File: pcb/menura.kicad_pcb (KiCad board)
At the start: 2 copper layers, 123.3 x 97.2 mm, 54 parts, among them SW1 SW_Push, SW10 SW_Push, SW11 SW_Push, SW12 SW_Push, SW13 SW_Push, SW14 SW_Push, SW15 SW_Push, SW16 SW_Push, SW17 SW_Push, SW18 SW_Push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

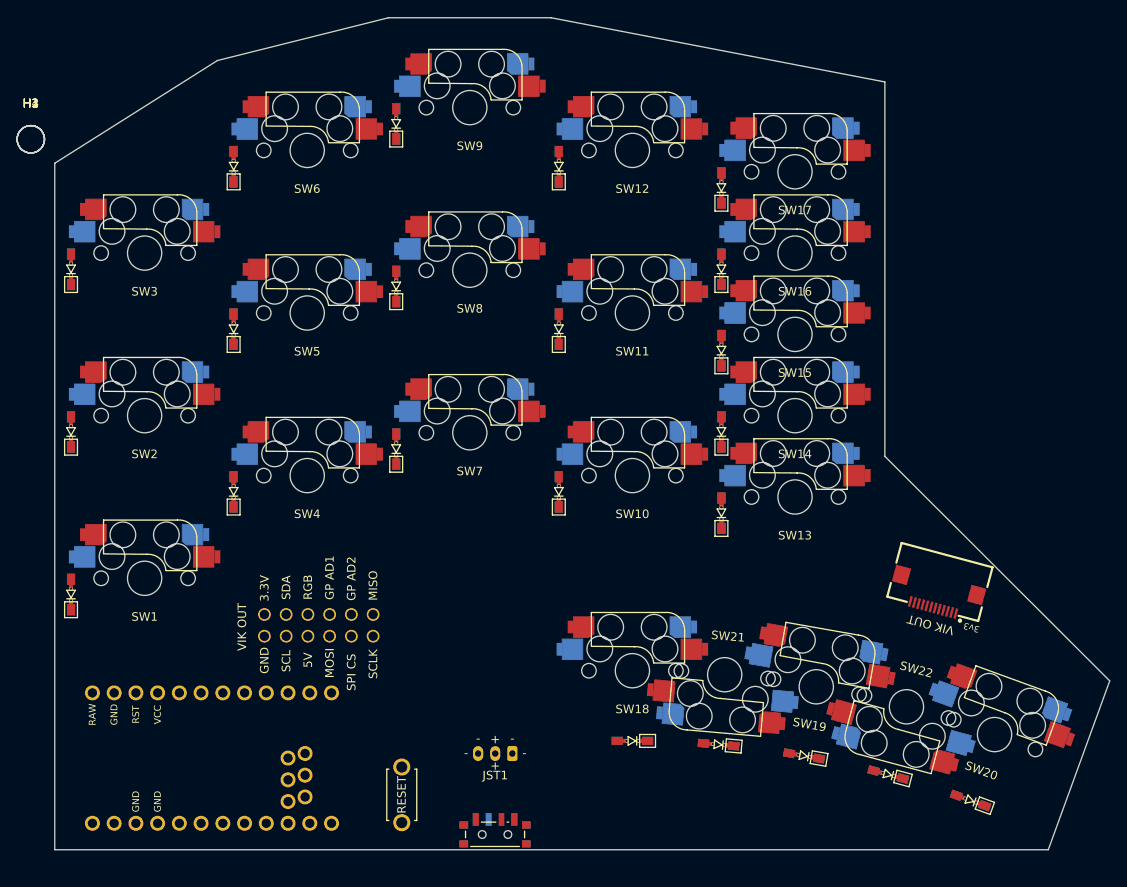
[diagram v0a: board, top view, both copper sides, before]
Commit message: adjust vik position and rotation
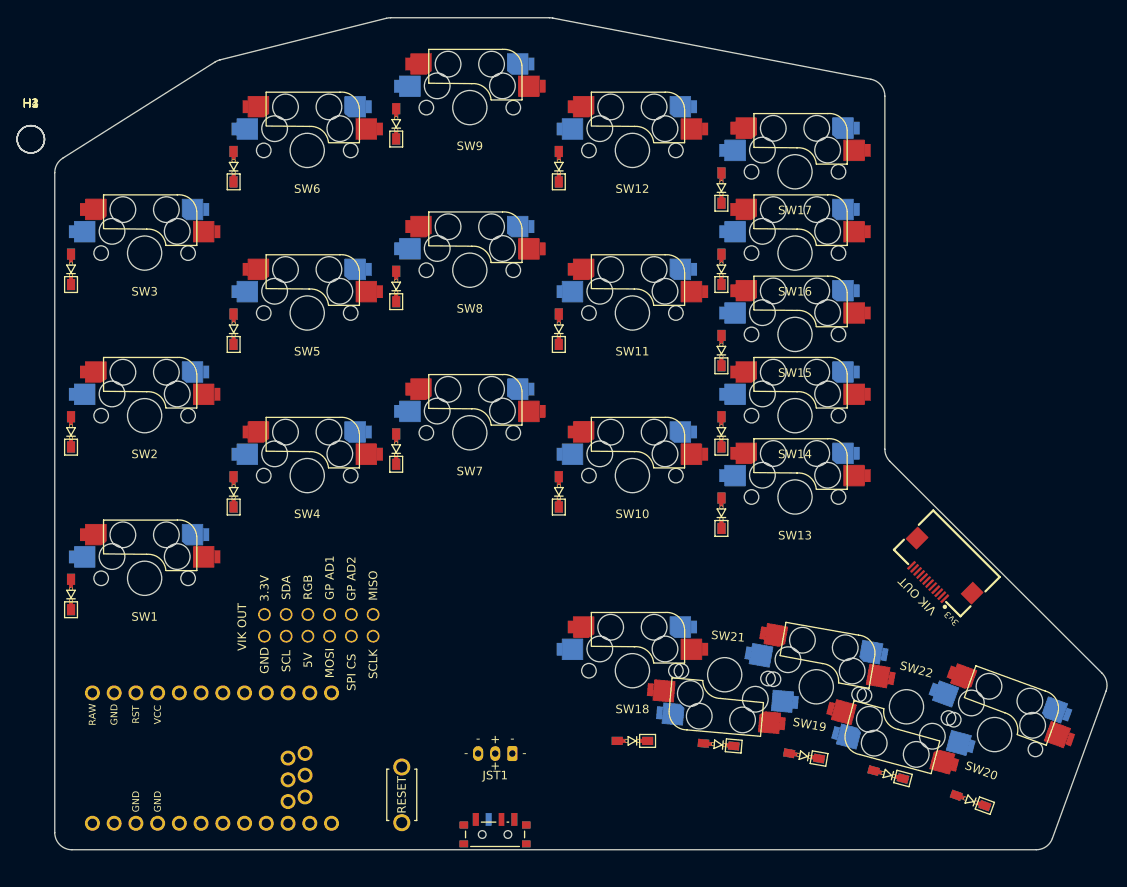
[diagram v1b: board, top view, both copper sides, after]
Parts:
- moved VIK1 2.47 mm to (193.0, 99.0), turned to 135 degrees
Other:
- board size 123.3 x 97.2 mm -> 123 x 97.2 mm

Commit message: shuffle few components around
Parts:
- moved JST1 28.0 mm to (116.5, 104.3), turned to 90 degrees
- moved VIK2 19.3 mm to (135.5, 115.5), turned to -90 degrees
- moved RSW1 13.0 mm to (142.3, 129.7), turned to 0 degrees
- moved PWR1 9.52 mm to (131.4, 129.9)

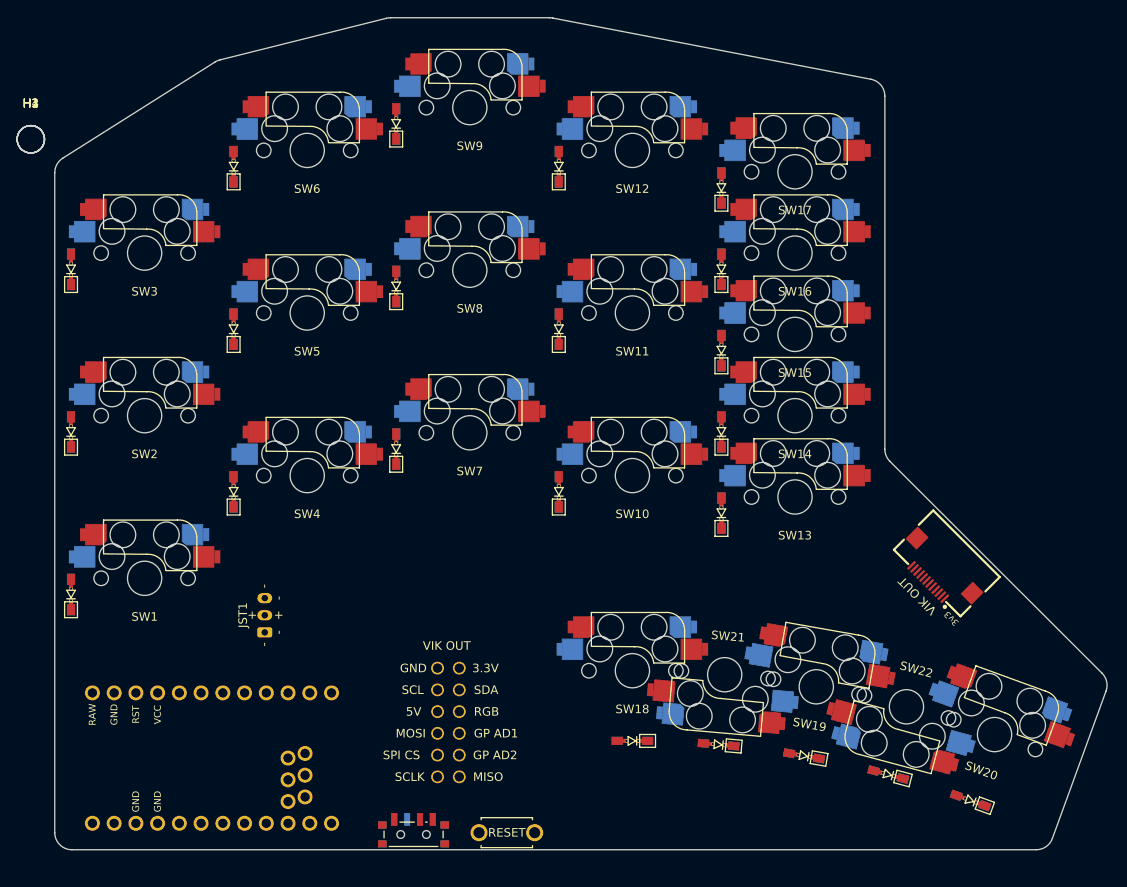
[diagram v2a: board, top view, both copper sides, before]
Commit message: tweak urchin diode footprint, add tenting puck footprints
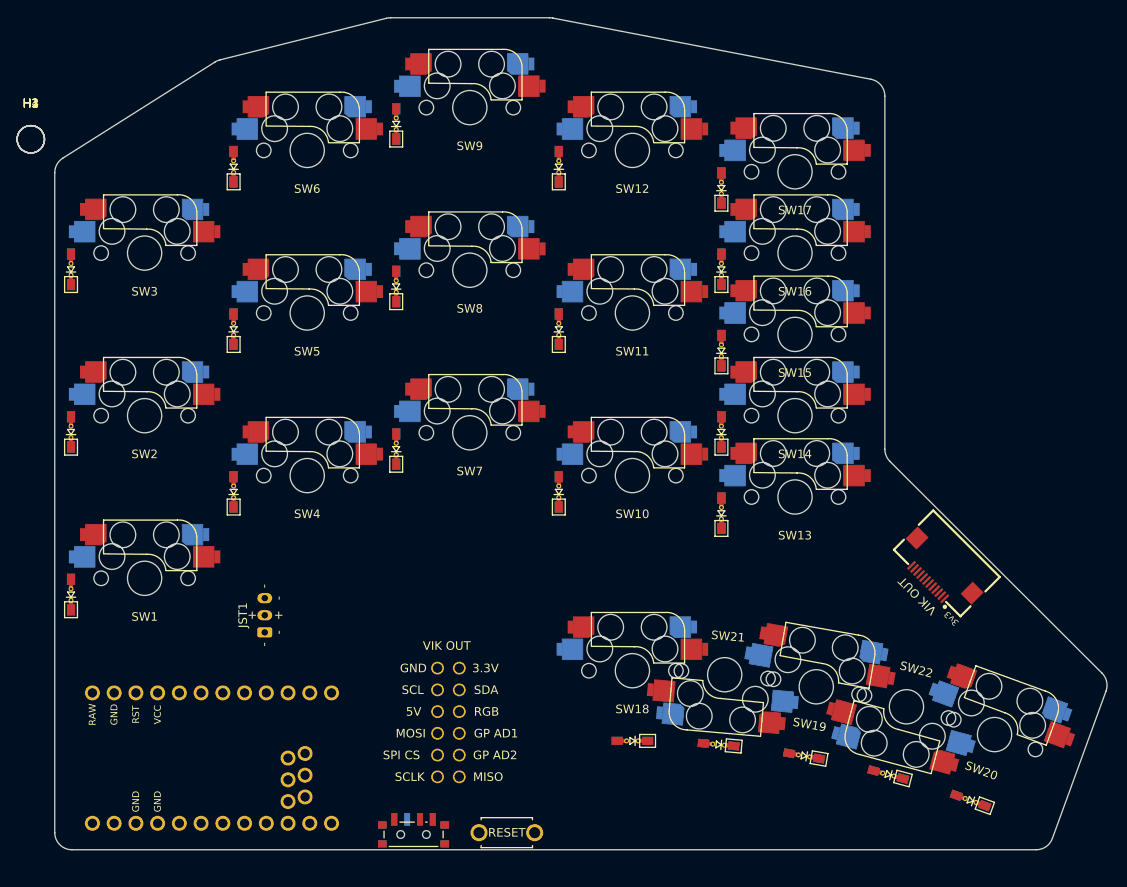
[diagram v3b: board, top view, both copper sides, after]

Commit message: logo silkscreens
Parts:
- added LOGO1: menura, quappo:Logo_menura, F.Cu at (167.3, 129.7)
- added LOGO2: vik, quappo:Logo_vik-small, F.Cu at (200.7, 105.4)

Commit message: holes
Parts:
- D1, D10, D11, D12, D13, D14, D15, D16, D17, D18, D19, D2, D20, D21, D22, D3, D4, D5, D6, D7, D8, D9: value 1N4148W -> (none); footprint quappo:Diode_SMD-reversible-urchin -> ComboDiode
- H1, H2, H3, H4: value MountingHole -> (none); footprint MountingHole:MountingHole_3.2mm_M3 -> SMDPad
- JST1: value Conn_01x03_Socket -> (none); footprint quappo:Connector_JST-PH-3prong -> JST_PH_S2B-PH-K_02x2.00mm_Angled
- LOGO1: value menura -> (none); footprint quappo:Logo_menura -> SMDPad
- LOGO2: value vik -> (none); footprint quappo:Logo_vik-small -> SMDPad
- MCU1: value N!N -> (none); footprint quappo:MCU_nice-nano -> ProMicro
- PWR1: value SW_SPDT -> (none); footprint quappo:Switch_power-reversible-kim -> E73:SPDT_C128955
- RSW1: value SW_Push -> (none); footprint quappo:Switch_reset-2pin -> E73:SW_TACT_ALPS_SKQGABE010
- SW1, SW10, SW11, SW12, SW13, SW14, SW15, SW16, SW17, SW18, SW19, SW2, SW20, SW21, SW22, SW3, SW4, SW5, SW6, SW7, SW8, SW9: value SW_Push -> (none); footprint quappo:Switch_MX-hotswap-reversible -> MX
- VIK1: value ~ -> (none); footprint quappo:Connector_vik-keyboard-horizontal -> SMDPad
- VIK2: value ~ -> (none); footprint quappo:Connector_vik-keyboard-throughhole -> SMDPad
- moved LOGO2 47.5 mm to (157.3, 124.7), turned to 360 degrees
- moved VIK1 5.66 mm to (197.0, 103.0)
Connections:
- D1 pad 1: row2 -> (no net)
- D1 pad 2: Net-(D1-A) -> (no net)
- D10 pad 1: row2 -> (no net)
- D10 pad 2: Net-(D10-A) -> (no net)
- D11 pad 1: row1 -> (no net)
- D11 pad 2: Net-(D11-A) -> (no net)
- D12 pad 1: row0 -> (no net)
- D12 pad 2: Net-(D12-A) -> (no net)
- D13 pad 1: row2 -> (no net)
- D13 pad 2: Net-(D13-A) -> (no net)
- D14 pad 1: row1 -> (no net)
- D14 pad 2: Net-(D14-A) -> (no net)
- D15 pad 1: row1 -> (no net)
- D15 pad 2: Net-(D15-A) -> (no net)
- D16 pad 1: row0 -> (no net)
- D16 pad 2: Net-(D16-A) -> (no net)
- D17 pad 1: row0 -> (no net)
- D17 pad 2: Net-(D17-A) -> (no net)
- D18 pad 1: row3 -> (no net)
- D18 pad 2: Net-(D18-A) -> (no net)
- D19 pad 1: row3 -> (no net)
- D19 pad 2: Net-(D19-A) -> (no net)
- D2 pad 1: row1 -> (no net)
- D2 pad 2: Net-(D2-A) -> (no net)
- D20 pad 1: row3 -> (no net)
- D20 pad 2: Net-(D20-A) -> (no net)
- D21 pad 1: row3 -> (no net)
- D21 pad 2: Net-(D21-A) -> (no net)
- D22 pad 1: row3 -> (no net)
- D22 pad 2: Net-(D22-A) -> (no net)
- D3 pad 1: row0 -> (no net)
- D3 pad 2: Net-(D3-A) -> (no net)
- D4 pad 1: row2 -> (no net)
- D4 pad 2: Net-(D4-A) -> (no net)
- D5 pad 1: row1 -> (no net)
- D5 pad 2: Net-(D5-A) -> (no net)
- D6 pad 1: row0 -> (no net)
- D6 pad 2: Net-(D6-A) -> (no net)
- D7 pad 1: row2 -> (no net)
- D7 pad 2: Net-(D7-A) -> (no net)
- D8 pad 1: row1 -> (no net)
- D8 pad 2: Net-(D8-A) -> (no net)
- D9 pad 1: row0 -> (no net)
- D9 pad 2: Net-(D9-A) -> (no net)
- JST1 pad 1: GND -> (no net)
- JST1 pad 2: Net-(JST1-Pin_2) -> (no net)
- MCU1 pad 1: unconnected-(MCU1-006-Pad1) -> RAW
- MCU1 pad 10: CS -> P14
- MCU1 pad 11: col4 -> P16
- MCU1 pad 12: row3 -> P10
- MCU1 pad 13: col3 -> P1
- MCU1 pad 14: col2 -> P0
- MCU1 pad 15: col1 -> GND
- MCU1 pad 16: col0 -> GND
- MCU1 pad 17: VIK_GPIO2 -> P2
- MCU1 pad 18: VIK_GPIO1 -> P3
- MCU1 pad 19: row2 -> P4
- MCU1 pad 2: row0 -> GND
- MCU1 pad 20: row1 -> P5
- MCU1 pad 21: +3.3V -> P6
- MCU1 pad 22: RST -> P7
- MCU1 pad 23: GND -> P8
- MCU1 pad 24: RAW -> P9
- MCU1 pad 3: GND -> RST
- MCU1 pad 4: GND -> VCC
- MCU1 pad 5: SDA -> P21
- MCU1 pad 6: SCL -> P20
- MCU1 pad 7: SCLK -> P19
- MCU1 pad 8: MISO -> P18
- MCU1 pad 9: MOSI -> P15
- PWR1 pad 1: RAW -> (no net)
- PWR1 pad 2: Net-(JST1-Pin_2) -> (no net)
- PWR1 pad 3: unconnected-(PWR1-C-Pad3)_0 -> (no net)
- RSW1 pad 1: GND -> (no net)
- RSW1 pad 2: RST -> (no net)
- SW1 pad 1: col0 -> (no net)
- SW1 pad 2: Net-(D1-A) -> (no net)
- SW10 pad 1: col3 -> (no net)
- SW10 pad 2: Net-(D10-A) -> (no net)
- SW11 pad 1: col3 -> (no net)
- SW11 pad 2: Net-(D11-A) -> (no net)
- SW12 pad 1: col3 -> (no net)
- SW12 pad 2: Net-(D12-A) -> (no net)
- SW13 pad 1: col4 -> (no net)
- SW13 pad 2: Net-(D13-A) -> (no net)
- SW14 pad 1: col4 -> (no net)
- SW14 pad 2: Net-(D14-A) -> (no net)
- SW15 pad 1: col4 -> (no net)
- SW15 pad 2: Net-(D15-A) -> (no net)
- SW16 pad 1: col4 -> (no net)
- SW16 pad 2: Net-(D16-A) -> (no net)
- SW17 pad 1: col4 -> (no net)
- SW17 pad 2: Net-(D17-A) -> (no net)
- SW18 pad 1: col2 -> (no net)
- SW18 pad 2: Net-(D18-A) -> (no net)
- SW19 pad 1: col3 -> (no net)
- SW19 pad 2: Net-(D19-A) -> (no net)
- SW2 pad 1: col0 -> (no net)
- SW2 pad 2: Net-(D2-A) -> (no net)
- SW20 pad 1: col4 -> (no net)
- SW20 pad 2: Net-(D20-A) -> (no net)
- SW21 pad 1: col2 -> (no net)
- SW21 pad 2: Net-(D21-A) -> (no net)
- SW22 pad 1: col3 -> (no net)
- SW22 pad 2: Net-(D22-A) -> (no net)
- SW3 pad 1: col0 -> (no net)
- SW3 pad 2: Net-(D3-A) -> (no net)
- SW4 pad 1: col1 -> (no net)
- SW4 pad 2: Net-(D4-A) -> (no net)
- SW5 pad 1: col1 -> (no net)
- SW5 pad 2: Net-(D5-A) -> (no net)
- SW6 pad 1: col1 -> (no net)
- SW6 pad 2: Net-(D6-A) -> (no net)
- SW7 pad 1: col2 -> (no net)
- SW7 pad 2: Net-(D7-A) -> (no net)
- SW8 pad 1: col2 -> (no net)
- SW8 pad 2: Net-(D8-A) -> (no net)
- SW9 pad 1: col2 -> (no net)
- SW9 pad 2: Net-(D9-A) -> (no net)
- VIK1 pad 1: +3.3V -> (no net)
- VIK2 pad 1: +3.3V -> (no net)
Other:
- net class Default added: clearance 0.2, trace_width 0.25, via_dia 0.8, via_drill 0.4
